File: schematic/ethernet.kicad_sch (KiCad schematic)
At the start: 38 parts, among them J1 ARJP11A-MASA-B-A-EMU2, U3 W5500, Y2 25MHz 12pF YXC

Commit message: Assign LCSC part numbers, mark PS1 DNP for JLC assembly
Every BOM line except PS1 now carries an LCSC field. Generic passives
move to JLC basic parts with equal or better ratings. Parts not stocked
at LCSC are swapped: C1/C2 to T520D227M010ATE018 (10 V), F1 to
0805L035/24XR, J8 to a generic gold 2x6 header, D6 to SMF3.3A.
PS1 (Ag9905MT) is DNP: bought separately and hand-soldered.
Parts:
- C10, C11, C5, C6, C7, C8, C9: LCSC (none) -> C1525; MANUFACTURER YAGEO -> Samsung Electro-Mechanics; MPN CC0402KRX7R7BB104 -> CL05B104KO5NNNC
- C26, C27: LCSC (none) -> C1549; MANUFACTURER YAGEO -> FH; MPN CC0402JRNPO9BN180 -> 0402CG180J500NT
- C28, C29: LCSC (none) -> C93654
- C30: LCSC (none) -> C19666
- C31, C35: LCSC (none) -> C15195; MANUFACTURER YAGEO -> Samsung Electro-Mechanics; MPN CC0402KRX7R9BB103 -> CL05B103KB5NNNC
- C32: LCSC (none) -> C15850
- C34: LCSC (none) -> C1532; MANUFACTURER YAGEO -> FH; MPN CC0402KRX7R9BB223 -> 0402B223K500NT
- C36: LCSC (none) -> C2167446
- J1: LCSC (none) -> C6125670
- L2: LCSC (none) -> C14709
- R10, R11, R12, R9: LCSC (none) -> C25105; MANUFACTURER YAGEO -> UNI-ROYAL; MPN RC0402FR-0733RL -> 0402WGF330JTCE
- R15: LCSC (none) -> C138060
- R16, R17, R18: LCSC (none) -> C25744
- R20, R21, R22, R23: LCSC (none) -> C25120; MANUFACTURER YAGEO -> UNI-ROYAL; MPN RC0402FR-0749R9L -> 0402WGF499JTCE
- R26: LCSC (none) -> C25077; MANUFACTURER YAGEO -> UNI-ROYAL; MPN RC0402FR-0710RL -> 0402WGF100JTCE
- R28: LCSC (none) -> C22935; MANUFACTURER YAGEO -> UNI-ROYAL; MPN RC0603FR-071ML -> 0603WAF1004T5E
- R29: LCSC (none) -> C26083; MANUFACTURER YAGEO -> UNI-ROYAL; MPN RC0402FR-071ML -> 0402WGF1004TCE
- R3, R4: LCSC (none) -> C25104; MANUFACTURER YAGEO -> UNI-ROYAL; MPN RC0402FR-07330RL -> 0402WGF3300TCE
- U3: LCSC (none) -> C32843
- Y2: LCSC (none) -> C9006

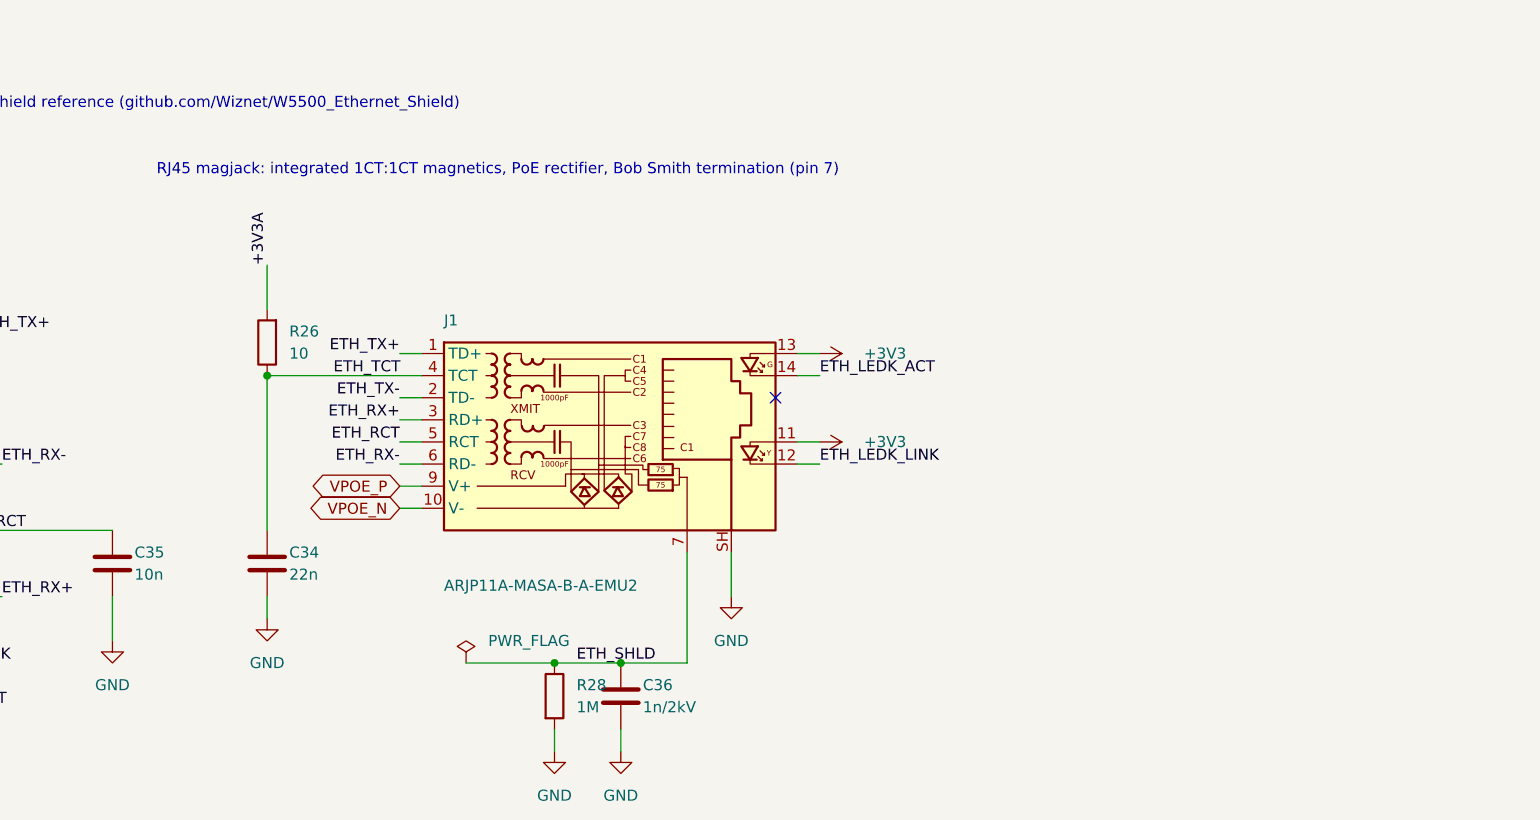
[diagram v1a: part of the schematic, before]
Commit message: Power from the 19 V bus instead of PoE
Drop the Ag9905MT PoE module and the ARJP11A PoE magjack. New J3
(JST PH 2p) takes the frame's redundant 19 V bus: F3 PTC, D1 SMAJ22A
TVS, D8 SS34 reverse-polarity diode, U8 LMR51430 buck (1.1 MHz,
3.3 uH, 100k/13k -> 5.22 V) into the existing D2/D3 5 V OR-ing.
J1 becomes a HanRun HR911105A plain magjack (pin 8 Bob Smith to GND,
shield to ETH_SHLD). All new parts have LCSC numbers.

Net classes PWR_POE/PWR_POE_5V become PWR_19V/PWR_BUCK_5V; the PoE
clearance DRU rule is removed. Specs and handoff updated.
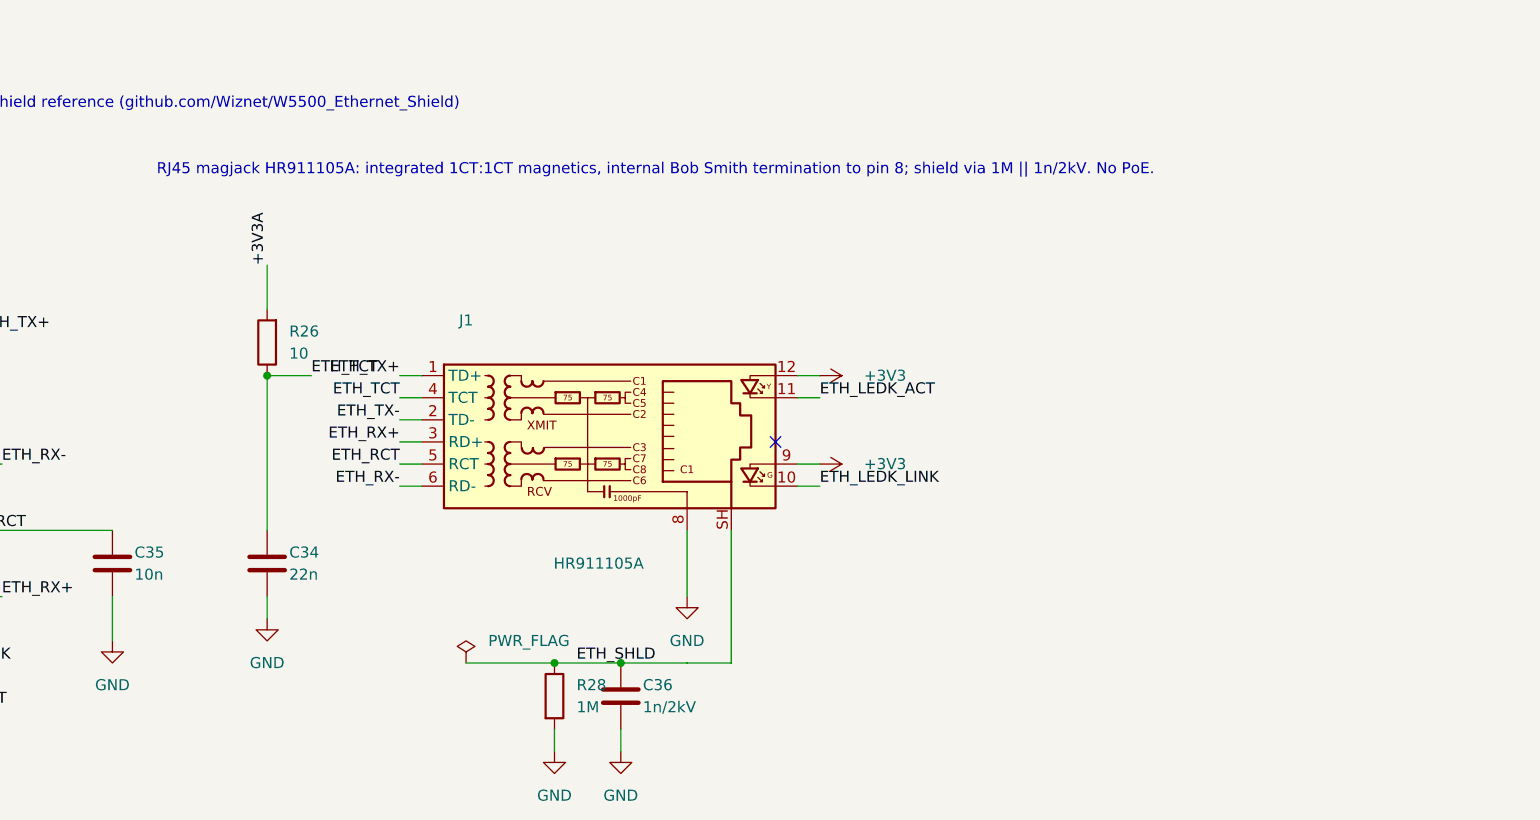
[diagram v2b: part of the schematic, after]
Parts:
- removed J1: ARJP11A-MASA-B-A-EMU2, Connector_RJ:RJ45_Abracon_ARJP11A-MA_Horizontal, symbol Connector:RJ45_Abracon_ARJP11A-MASA-B-A-EMU2
- added J1: HR911105A, Connector_RJ:RJ45_Hanrun_HR911105A_Horizontal, symbol Connector:RJ45_Hanrun_HR911105A_Horizontal
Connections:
- net +3V3: now also J1.12, J1.9
- net ETH_LEDK_ACT: now also J1.11
- net ETH_LEDK_LINK: now also J1.10
- net ETH_RCT: now also J1.5 (RCT)
- net ETH_RX+: now also J1.3 (RD+)
- net ETH_RX-: now also J1.6 (RD-)
- net ETH_SHLD: now also J1.SH
- net ETH_TCT: now also J1.4 (TCT)
- net ETH_TX+: now also J1.1 (TD+)
- net ETH_TX-: now also J1.2 (TD-)
- net GND: now also J1.8
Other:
- note added: "RJ45 magjack HR911105A: integrated 1CT:1CT magnetics, internal Bob Smith termination to pin 8; shield via 1M || 1n/2kV. No PoE."
- note removed: "RJ45 magjack: integrated 1CT:1CT magnetics, PoE rectifier, Bob Smith termination (pin 7)"

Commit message: R15: swap to UNI-ROYAL 0402WGF1242TCE (C11692)
Same 12.4k 1% 0402 for the W5500 EXRES; the YAGEO part (C138060) had 41
in stock at JLC against 8 needed for the first build, C11692 has ~89k.
MANUFACTURER, MPN and LCSC updated in the schematic and on the board.
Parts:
- R15: LCSC C138060 -> C11692; MANUFACTURER YAGEO -> UNI-ROYAL; MPN RC0402FR-0712K4L -> 0402WGF1242TCE
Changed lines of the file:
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@@
 			)
 		)
-		(property "MANUFACTURER" "YAGEO"
+		(property "MANUFACTURER" "UNI-ROYAL"
 			(at 152.4 130.81 0)
 			(hide yes)
@@
 			)
 		)
-		(property "MPN" "RC0402FR-0712K4L"
+		(property "MPN" "0402WGF1242TCE"
 			(at 152.4 130.81 0)
 			(hide yes)
@@
 			)
 		)
-		(property "LCSC" "C138060"
+		(property "LCSC" "C11692"
 			(at 152.4 130.81 0)
 			(hide yes)

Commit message: Fix the 2026-10 review findings
Schematic: NODE_ON8 to U15 GPB4 (GPA7 is output-only), F3 1206L075/33NR,
VBUS bleeder R65/C52, R38 12.4k (BUCK_5V 5.44 V), D9 SMAJ6.0A crowbar on
BUCK_5V, R101-R116 270R, C26/C27 15 pF, R39-R46 47k, D6 value.

Layout: hole-clearance rule with units (0.3 mm) and 6.5 mm keep-outs at
H1-H4, EN RC / decoupling / VIN_SENSE filter at U1, no F.Cu under the
module body, vias kept off the U1 EPAD, zones 1 mm from the short edges
for mouse-bite rails, silk 1.0/0.15 mm, autorouter vias moved out of
SMD pads (only the U1 pad 29 thermal vias remain).

tools/jlcfab.py: per-footprint rotation/centroid corrections checked
against EasyEDA footprints (K*, U2, U8, JST fixed; U1, J2 offsets), no
drill maps in the zip. Docs: controller.md, handoff, review status.

ERC 0; DRC 0 unconnected, 0 parity, 3 known violations.
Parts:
- C26, C27: value 18p -> 15p; LCSC C1549 -> C1548; MPN 0402CG180J500NT -> 0402CG150J500NT
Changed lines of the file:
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@@
 			)
 		)
-		(property "Value" "18p"
+		(property "Value" "15p"
 			(at 71.12 142.24 0)
 			(show_name no)
@@
 			)
 		)
-		(property "MPN" "0402CG180J500NT"
+		(property "MPN" "0402CG150J500NT"
 			(at 73.66 140.97 0)
 			(hide yes)
@@
 			)
 		)
-		(property "LCSC" "C1549"
+		(property "LCSC" "C1548"
 			(at 73.66 140.97 0)
 			(hide yes)
@@
 			)
 		)
-		(property "Value" "18p"
+		(property "Value" "15p"
 			(at 83.82 142.24 0)
 			(show_name no)
@@
 			)
 		)
-		(property "MPN" "0402CG180J500NT"
+		(property "MPN" "0402CG150J500NT"
 			(at 81.28 140.97 0)
 			(hide yes)
@@
 			)
 		)
-		(property "LCSC" "C1549"
+		(property "LCSC" "C1548"
 			(at 81.28 140.97 0)
 			(hide yes)

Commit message: C36: KEMET C1812C102KGRACTU (C2167446, out of stock) -> Yageo CC1812KKX7RDBB102 (C118019)
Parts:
- C36: LCSC C2167446 -> C118019; MPN C1812C102KGRACTU -> CC1812KKX7RDBB102
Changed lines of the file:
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@@
 			)
 		)
-		(property "MPN" "C1812C102KGRACTU"
+		(property "MPN" "CC1812KKX7RDBB102"
 			(at 243.84 120.65 0)
 			(hide yes)
@@
 			)
 		)
-		(property "LCSC" "C2167446"
+		(property "LCSC" "C118019"
 			(at 243.84 120.65 0)
 			(hide yes)
